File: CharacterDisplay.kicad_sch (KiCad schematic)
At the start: 6 parts, among them J4 Conn_01x16_Pin

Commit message: 3/8/2025
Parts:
- removed J4: Conn_01x16_Pin, symbol Connector:Conn_01x16_Pin
- removed R21, R27: 5k, symbol Device:R_US
- removed VR1: 3362P-1-103LF, jka_library:TRIM_3362P-1-103LF, symbol jka_library:3362P-1-103LF
- added C71, C72: 10 uF, Capacitor_SMD:C_0805_2012Metric, symbol Device:C
- added H1, H2, H3, H4: MountingHole, MountingHole:MountingHole_3.2mm_M3, symbol Mechanical:MountingHole
- added J15: Conn_01x16_Socket, Connector_PinSocket_2.54mm:PinSocket_1x16_P2.54mm_Vertical, symbol Connector:Conn_01x16_Socket
- added R46, R47: 5k, Resistor_SMD:R_0603_1608Metric, symbol Device:R_US
- added VR1: 23BR10KLFTR, jka_library:SOT_10KLFTR_BIT, symbol jka_library:23BR10KLFTR
- C18: renamed from C23; value C -> 1 uF; footprint (none) -> Capacitor_SMD:C_0805_2012Metric
- C19: renamed from C24; value C -> 1 uF; footprint (none) -> Capacitor_SMD:C_0805_2012Metric
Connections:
- net DB0: now also J15.7 (Pin_7)
- net DB1: now also J15.8 (Pin_8)
- net DB2: now also J15.9 (Pin_9)
- net DB3: now also J15.10 (Pin_10)
- net DB4: now also J15.11 (Pin_11)
- net DB5: now also J15.12 (Pin_12)
- net DB6: now also J15.13 (Pin_13)
- net DB7: now also J15.14 (Pin_14)
- net GND: now also C18.1, C71.1, C72.1, J15.1 (Pin_1), J15.16 (Pin_16), R47.2, VR1.3; no longer C18.2
- net LCD_EN: now also J15.6 (Pin_6)
- net REG_SEL: now also J15.4 (Pin_4)
- net R/W: now also J15.5 (Pin_5)
- net V0: now also J15.3 (Pin_3), R46.2, R47.1, VR1.2
- net +3.3V renamed +3V3
- net +3V3: now also C71.2, C72.2, J15.15 (Pin_15), J15.2 (Pin_2), R46.1, VR1.1; no longer C18.1
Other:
- moved on the sheet: C18, C19

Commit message: Layout draft complete
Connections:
- net +3V3: now also C18.2
- net DB0 renamed LCD_DB0
- net DB1 renamed LCD_DB1
- net DB2 renamed LCD_DB2
- net DB3 renamed LCD_DB3
- net REG_SEL renamed LCD_REG_SEL
- net R/W renamed LCD_R/W
- no-connect marks 0 -> 4
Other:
- note added: "Designed around the C204A-FTW-LW63 from Focus LCDs"
- title: (none) -> Jakka1
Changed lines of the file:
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@@
 	(generator_version "8.0")
 	(paper "A4")
+	(title_block
+		(title "Jakka1")
+		(rev "1")
+	)
+	(junction
+		(at 144.78 73.66)
+		(diameter 0)
+		(color 0 0 0 0)
+	)
+	(junction
+		(at 144.78 82.55)
+		(diameter 0)
+		(color 0 0 0 0)
+	)
 	(junction
 		(at 130.81 130.81)
@@
 	)
 	(junction
-		(at 144.78 81.28)
-		(diameter 0)
-		(color 0 0 0 0)
-	)
-	(junction
 		(at 130.81 121.92)
 		(diameter 0)
 		(color 0 0 0 0)
 	)
+	(no_connect
+		(at 154.94 111.76)
+	)
+	(no_connect
+		(at 154.94 116.84)
+	)
+	(no_connect
+		(at 154.94 114.3)
+	)
+	(no_connect
+		(at 154.94 119.38)
+	)
 	(wire
 		(pts
@@
 	(wire
 		(pts
+			(xy 144.78 73.66) (xy 157.48 73.66)
+		)
+		(stroke
+			(width 0)
+			(type default)
+		)
+	)
+	(wire
+		(pts
 			(xy 137.16 121.92) (xy 144.78 121.92)
 		)
@@
 	(wire
 		(pts
-			(xy 151.13 81.28) (xy 144.78 81.28)
+			(xy 151.13 82.55) (xy 144.78 82.55)
 		)
 		(stroke
@@
 	(wire
 		(pts
-			(xy 138.43 73.66) (xy 157.48 73.66)
+			(xy 138.43 73.66) (xy 144.78 73.66)
 		)
 		(stroke
@@
 	(wire
 		(pts
-			(xy 151.13 86.36) (xy 151.13 81.28)
+			(xy 151.13 86.36) (xy 151.13 82.55)
 		)
 		(stroke
@@
 	(text "C204A-FTW-LW63\n"
 		(exclude_from_sim no)
-		(at 202.184 95.758 0)
+		(at 210.312 119.634 0)
 		(effects
 			(font
@@
 	(text "20 x 4 LCD character display"
 		(exclude_from_sim no)
-		(at 202.438 91.694 0)
+		(at 211.074 100.584 0)
 		(effects
 			(font
 				(size 2.032 2.032)
+			)
+		)
+	)
+	(text "Designed around the C204A-FTW-LW63\nfrom Focus LCDs"
+		(exclude_from_sim no)
+		(at 210.058 114.3 0)
+		(effects
+			(font
+				(size 1.27 1.27)
 			)
 		)
@@
 		)
 	)
-	(hierarchical_label "LCD_EN"
+	(global_label "LCD_DB1"
+		(shape input)
+		(at 154.94 104.14 180)
+		(fields_autoplaced yes)
+		(effects
+			(font
+				(size 1.27 1.27)
+			)
+			(justify right)
+		)
+		(property "Intersheetrefs" "${INTERSHEET_REFS}"
+			(at 148.2053 104.14 0)
+			(effects
+				(font
+					(size 1.27 1.27)
+				)
+				(justify right)
+				(hide yes)
+			)
+		)
+	)
+	(global_label "LCD_DB0"
+		(shape input)
+		(at 154.94 101.6 180)
+		(fields_autoplaced yes)
+		(effects
+			(font
+				(size 1.27 1.27)
+			)
+			(justify right)
+		)
+		(property "Intersheetrefs" "${INTERSHEET_REFS}"
+			(at 148.2053 101.6 0)
+			(effects
+				(font
+					(size 1.27 1.27)
+				)
+				(justify right)
+				(hide yes)
+			)
+		)
+	)
+	(global_label "LCD_R{slash}W"
+		(shape input)
+		(at 154.94 96.52 180)
+		(fields_autoplaced yes)
+		(effects
+			(font
+				(size 1.27 1.27)
+			)
+			(justify right)
+		)
+		(property "Intersheetrefs" "${INTERSHEET_REFS}"
+			(at 143.3672 96.52 0)
+			(effects
+				(font
+					(size 1.27 1.27)
+				)
+				(justify right)
+				(hide yes)
+			)
+		)
+	)
+	(global_label "LCD_DB3"
+		(shape input)
+		(at 154.94 109.22 180)
+		(fields_autoplaced yes)
+		(effects
+			(font
+				(size 1.27 1.27)
+			)
+			(justify right)
+		)
+		(property "Intersheetrefs" "${INTERSHEET_REFS}"
+			(at 143.6696 109.22 0)
+			(effects
+				(font
+					(size 1.27 1.27)
+				)
+				(justify right)
+				(hide yes)
+			)
+		)
+	)
+	(global_label "LCD_EN"
 		(shape input)
 		(at 154.94 99.06 180)
@@
 			(justify right)
 		)
-	)
-	(hierarchical_label "DB3"
+		(property "Intersheetrefs" "${INTERSHEET_REFS}"
+			(at 144.9396 99.06 0)
+			(effects
+				(font
+					(size 1.27 1.27)
+				)
+				(justify right)
+				(hide yes)
+			)
+		)
+	)
+	(global_label "LCD_DB2"
 		(shape input)
-		(at 154.94 109.22 180)
+		(at 154.94 106.68 180)
 		(fields_autoplaced yes)
 		(effects
@@
 			)
 			(justify right)
+		)
+		(property "Intersheetrefs" "${INTERSHEET_REFS}"
+			(at 148.2053 106.68 0)
+			(effects
+				(font
+					(size 1.27 1.27)
+				)
+				(justify right)
+				(hide yes)
+			)
+		)
+	)
+	(global_label "LCD_REG_SEL"
+		(shape input)
+		(at 154.94 93.98 180)
+		(fields_autoplaced yes)
+		(effects
+			(font
+				(size 1.27 1.27)
+			)
+			(justify right)
+		)
+		(property "Intersheetrefs" "${INTERSHEET_REFS}"
+			(at 143.9116 93.98 0)
+			(effects
+				(font
+					(size 1.27 1.27)
+				)
+				(justify right)
+				(hide yes)
+			)
 		)
 	)
@@
 		(fields_autoplaced yes)
 		(effects
-			(font
-				(size 1.27 1.27)
-			)
-			(justify right)
-		)
-	)
-	(hierarchical_label "DB0"
-		(shape input)
-		(at 154.94 101.6 180)
-		(fields_autoplaced yes)
-		(effects
-			(font
-				(size 1.27 1.27)
-			)
-			(justify right)
-		)
-	)
-	(hierarchical_label "R{slash}W"
-		(shape input)
-		(at 154.94 96.52 180)
-		(fields_autoplaced yes)
-		(effects
-			(font
-				(size 1.27 1.27)
-			)
-			(justify right)
-		)
-	)
-	(hierarchical_label "DB5"
-		(shape input)
-		(at 154.94 114.3 180)
-		(fields_autoplaced yes)
-		(effects
-			(font
-				(size 1.27 1.27)
-			)
-			(justify right)
-		)
-	)
-	(hierarchical_label "REG_SEL"
-		(shape input)
-		(at 154.94 93.98 180)
-		(fields_autoplaced yes)
-		(effects
-			(font
-				(size 1.27 1.27)
-			)
-			(justify right)
-		)
-	)
-	(hierarchical_label "DB7"
-		(shape input)
-		(at 154.94 119.38 180)
-		(fields_autoplaced yes)
-		(effects
-			(font
-				(size 1.27 1.27)
-			)
-			(justify right)
-		)
-	)
-	(hierarchical_label "DB6"
-		(shape input)
-		(at 154.94 116.84 180)
-		(fields_autoplaced yes)
-		(effects
-			(font
-				(size 1.27 1.27)
-			)
-			(justify right)
-		)
-	)
-	(hierarchical_label "DB2"
-		(shape input)
-		(at 154.94 106.68 180)
-		(fields_autoplaced yes)
-		(effects
-			(font
-				(size 1.27 1.27)
-			)
-			(justify right)
-		)
-	)
-	(hierarchical_label "DB4"
-		(shape input)
-		(at 154.94 111.76 180)
-		(fields_autoplaced yes)
-		(effects
-			(font
-				(size 1.27 1.27)
-			)
-			(justify right)
-		)
-	)
-	(hierarchical_label "DB1"
-		(shape input)
-		(at 154.94 104.14 180)
-		(fields_autoplaced yes)
-		(effects

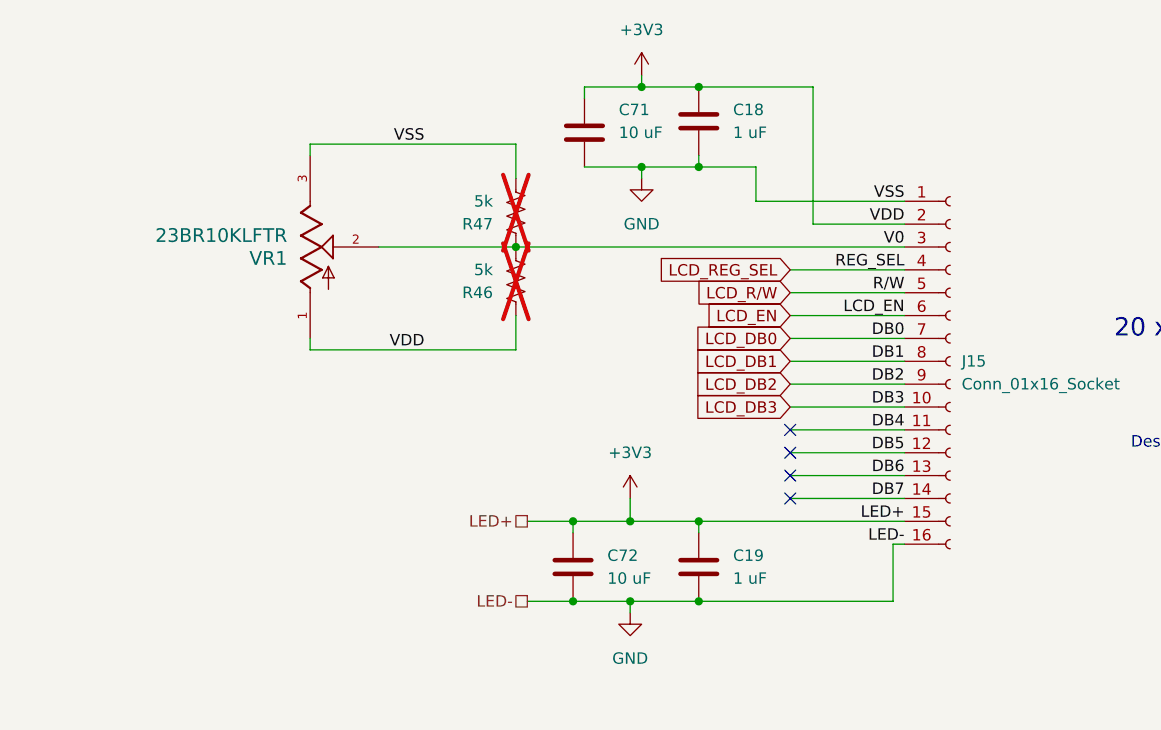
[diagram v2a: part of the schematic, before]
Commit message: First draft of design output, schematic, and layout complete
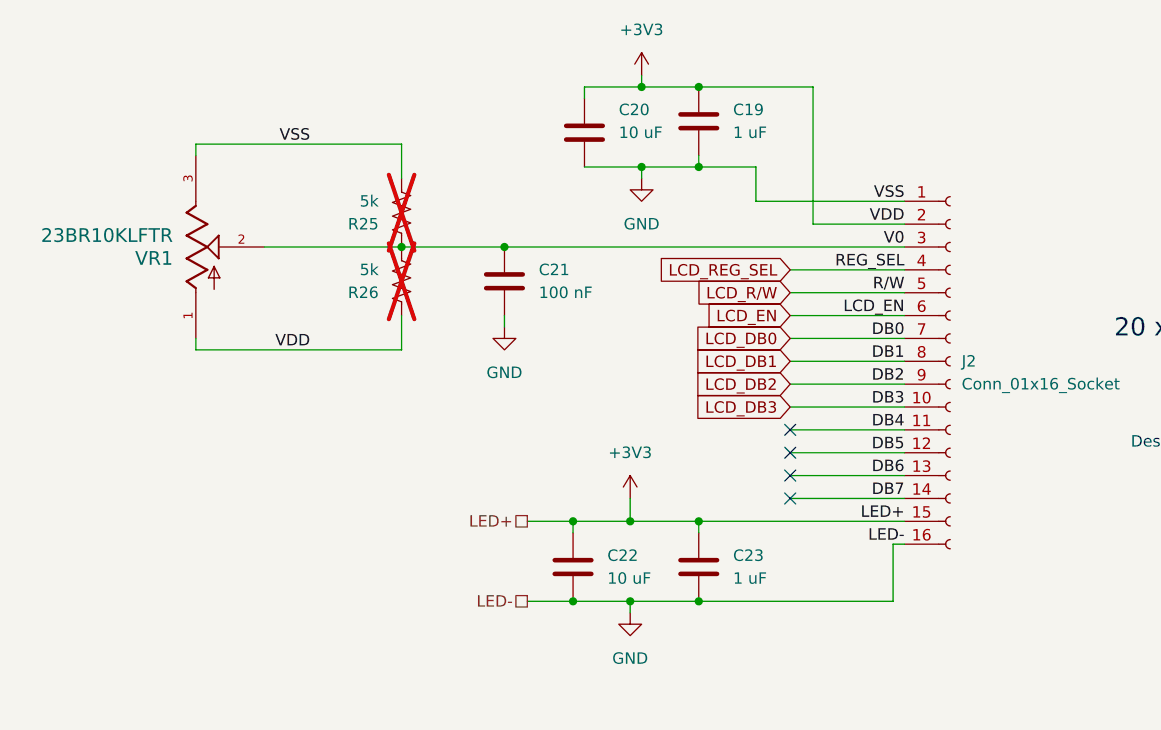
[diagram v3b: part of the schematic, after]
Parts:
- added C21: 100 nF, Capacitor_SMD:C_0603_1608Metric, symbol Device:C
- renumbered C18 to C19, C71 to C20, C72 to C22, C19 to C23, J15 to J2, R47 to R25, R46 to R26
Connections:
- net GND: now also C21.1
- net V0: now also C21.2
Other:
- company: (none) -> Jacob Kapala
- moved on the sheet: R25, R26, VR1
